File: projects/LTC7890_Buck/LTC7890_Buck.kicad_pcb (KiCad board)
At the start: 4 copper layers, 86 x 54 mm, 94 parts, among them J1 Bat In, J2 24V Out, J3 I2C Socket, J4 I2C Socket, Q1 IGC025S08S1, Q2 IGC025S08S1, Q3 IGC025S08S1, Q4 IGC025S08S1, SW1 Addr_Switch, SW2 Addr_Switch, U1 LTC7890, U2 TLV74033, U3 INA226

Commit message: Finished PCB
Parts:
- added C16: 100nF, Capacitor_SMD:C_0603_1608Metric, F.Cu at (148.5, 103.2)
- added C17: 100nF, Capacitor_SMD:C_0603_1608Metric, F.Cu at (150.0, 103.2)
- added C26: 100nF, Capacitor_SMD:C_0603_1608Metric, F.Cu at (130.0, 103.2)
- added C27: 100nF, Capacitor_SMD:C_0603_1608Metric, F.Cu at (131.5, 103.2)
- added C31: 100nF, Capacitor_SMD:C_0603_1608Metric, F.Cu at (140.8, 112.5)
- added C42: 100nF, Capacitor_SMD:C_0603_1608Metric, B.Cu at (140.0, 111.0)
- added NT1: NetTie_2, footprints:NetTie-2_SMD_Pad0.25mm, F.Cu at (139.8, 104.5)
- R14, R7: value 47 -> 100
- R15, R19, R3, R5: value 0 -> 1
- U3: footprint Package_SO:VSSOP-10_3x3mm_P0.5mm -> Package_SO:TSSOP-10_3x3mm_P0.5mm
- moved C35 23.5 mm to (137.2, 104.2), turned to 90 degrees
- moved C34 23.5 mm to (142.8, 104.2), turned to -90 degrees
- moved R14 22.2 mm to (138.8, 103.0), turned to 90 degrees
- moved R7 22.2 mm to (141.2, 103.0), turned to 90 degrees
- moved C22 7.57 mm to (124.0, 103.2)
- moved R30 6.02 mm to (145.2, 115.0)
- moved C23 4.61 mm to (125.5, 103.2)
- moved R25 4.53 mm to (136.2, 115.0)
- moved R31 4.53 mm to (142.2, 115.0)
- moved R34 4.26 mm to (155.5, 97.8), turned to -90 degrees
- moved R35 4.26 mm to (154.0, 97.8), turned to -90 degrees
- moved R5 3.89 mm to (146.0, 114.8)
- moved R19 3.48 mm to (134.0, 115.2)
- moved R20 3.48 mm to (134.0, 113.8)
- moved R6 3.26 mm to (146.0, 113.2)
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- renumbered C19 to C18, C20 to C19, C21 to C20, C22 to C21, C23 to C22, C24 to C23, C25 to C24, C26 to C25, C16 to C28, C17 to C29, C18 to C30, C27 to C32, C28 to C33, C29 to C34, C30 to C35, C31 to C36, C32 to C37, C33 to C38, C34 to C39, C35 to C40, C36 to C41, C37 to C43, C38 to C44, R18 to R17, R17 to R18
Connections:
- C1 pad 2: GND -> GNDPWR
- C10 pad 1: GND -> GNDPWR
- C11 pad 1: GND -> GNDPWR
- C12 pad 2: GND -> GNDPWR
- C13 pad 2: GND -> GNDPWR
- C14 pad 2: GND -> GNDPWR
- C15 pad 2: GND -> GNDPWR
- C18 pad 1: GND -> GNDPWR
- C19 pad 1: GND -> GNDPWR
- C2 pad 2: GND -> GNDPWR
- C20 pad 1: GND -> GNDPWR
- C21 pad 1: GND -> GNDPWR
- C22 pad 1: GND -> GNDPWR
- C23 pad 1: GND -> GNDPWR
- C24 pad 1: GND -> GNDPWR
- C25 pad 1: GND -> GNDPWR
- C28 pad 2: GND -> GNDPWR
- C29 pad 2: GND -> GNDPWR
- C3 pad 2: GND -> GNDPWR
- C30 pad 2: GND -> GNDPWR
- C33 pad 1: GND -> GNDPWR
- C36 pad 1: GND -> GNDA
- C37 pad 2: GND -> GNDA
- C38 pad 2: GND -> GNDA
- C4 pad 1: GND -> GNDPWR
- C40 pad 2: GND -> GNDA
- C41 pad 2: GND -> GNDA
- C43 pad 1: GND -> GNDA
- C5 pad 1: GND -> GNDPWR
- C6 pad 1: GND -> GNDPWR
- C7 pad 1: GND -> GNDPWR
- C8 pad 1: GND -> GNDPWR
- C9 pad 1: GND -> GNDPWR
- D1 pad 1: GND -> GNDA
- J1 pad : (no net) -> GNDPWR
- J1 pad 1: GND -> GNDPWR
- J2 pad : (no net) -> GNDPWR
- J2 pad 1: GND -> GNDPWR
- J3 pad 2: GND -> GNDA
- J3 pad MP: (no net) -> VDD
- J4 pad 2: GND -> GNDA
- J4 pad MP: (no net) -> VDD
- L1 pad 1: Net-(Q1-SS) -> Net-(L1-Pad1)
- L2 pad 2: Net-(Q3-SS) -> Net-(L2-Pad2)
- Q1 pad 3: Net-(Q1-SS) -> Net-(L1-Pad1)
- Q1 pad 5: Net-(Q1-SS) -> Net-(L1-Pad1)
- Q2 pad 2: Net-(Q1-SS) -> Net-(L1-Pad1)
- Q2 pad 3: GND -> GNDPWR
- Q2 pad 4: Net-(Q1-SS) -> Net-(L1-Pad1)
- Q2 pad 5: GND -> GNDPWR
- Q2 pad 6: GND -> GNDPWR
- Q3 pad 3: Net-(Q3-SS) -> Net-(L2-Pad2)
- Q3 pad 5: Net-(Q3-SS) -> Net-(L2-Pad2)
- Q4 pad 2: Net-(Q3-SS) -> Net-(L2-Pad2)
- Q4 pad 3: GND -> GNDPWR
- Q4 pad 4: Net-(Q3-SS) -> Net-(L2-Pad2)
- Q4 pad 5: GND -> GNDPWR
- Q4 pad 6: GND -> GNDPWR
- R16 pad 2: GND -> GNDA
- R2 pad 1: GND -> GNDA
- R9 pad 1: GND -> GNDA
- SW1 pad : (no net) -> GNDPWR
- SW1 pad 1: GND -> GNDA
- SW2 pad : (no net) -> GNDPWR
- SW2 pad 1: GND -> GNDA
- TP2 pad 1: GND -> GNDPWR
- TP4 pad 1: GND -> GNDPWR
- U1 pad 14: GND -> GNDA
- U1 pad 15: GND -> GNDA
- U1 pad 26: +24V -> VOUT
- U1 pad 3: GND -> GNDA
- U1 pad 41: GND -> GNDPWR
- U1 pad 6: GND -> GNDA
- U1 pad 7: GND -> unconnected-(U1-DRVUV-Pad7)
- U1 pad 8: GND -> GNDA
- U2 pad 2: GND -> GNDA
- U3 pad 7: GND -> GNDA
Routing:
- net Net-(J3-Pin_3): track 0.00 -> 88.3 mm, vias 0 -> 3
- net GNDA: track 0.00 -> 87.9 mm, vias 0 -> 8
- net Net-(J3-Pin_4): track 0.00 -> 84.2 mm, vias 0 -> 3
- net VOUT: track 0.00 -> 80.6 mm, vias 0 -> 6
- net +3.3V: track 0.00 -> 61.3 mm, vias 0 -> 2
- net +5V: track 0.00 -> 42.8 mm, vias 0 -> 3
- net /R-: track 0.00 -> 38.4 mm, vias 0 -> 2
- net Net-(U3-A0): track 0.00 -> 37.5 mm, vias 0 -> 1
- net Net-(L2-Pad1): track 0.00 -> 36.3 mm, vias 0 -> 2
- net Net-(L1-Pad2): track 0.00 -> 34.4 mm, vias 0 -> 2
- net /R+: track 0.00 -> 34.3 mm, vias 0 -> 2
- net Net-(U3-A1): track 0.00 -> 20.3 mm
- net /~{Alert}: track 0.00 -> 18.4 mm, vias 0 -> 2
- net VDD: track 0.00 -> 12.0 mm, vias 0 -> 27
- net Net-(R25-Pad1): track 0.00 -> 11.0 mm, vias 0 -> 2
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- added copper zone on B.Cu, net +24V
- added copper zone on F.Cu, net +24V
- added copper zone on B.Cu, net GNDA
- added copper zone on F.Cu, net GNDA
- added copper zone on B.Cu, net GNDPWR
- added copper zone on F.Cu, net GNDPWR
- added copper zone on In1.Cu, net GNDPWR
- added copper zone on In2.Cu, net GNDPWR
- added copper zone on F.Cu, net Net-(L1-Pad1)
- added copper zone on F.Cu, net Net-(L2-Pad2)
- added copper zone on F.Cu, net Net-(Q1-G)
- added copper zone on F.Cu, net Net-(Q1-SS)
- added copper zone on F.Cu, net Net-(Q2-G)
- added copper zone on F.Cu, net Net-(Q3-G)
- added copper zone on F.Cu, net Net-(Q3-SS)
- added copper zone on F.Cu, net Net-(Q4-G)
- added copper zone on B.Cu, net VDD
- added copper zone on F.Cu, net VDD
- added copper zone on B.Cu, net VOUT

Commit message: Minor changes
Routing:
- net GNDA: track 87.9 -> 86.7 mm
- net GNDPWR: vias 222 -> 226
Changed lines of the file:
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@@
 		(at 148.75 121.5 90)
 		(property "Reference" "R26"
-			(at 4.5 -2 0)
+			(at -4.5 -2 0)
 			(unlocked yes)
 			(layer "B.SilkS")
@@
 		(at 135.25 121.5 90)
 		(property "Reference" "R29"
-			(at 4.5 -1.75 0)
+			(at -4.5 -1.75 0)
 			(unlocked yes)
 			(layer "B.SilkS")
@@
 		(at 144.25 121.5 90)
 		(property "Reference" "R27"
-			(at 4.5 -2 0)
+			(at -4.5 -2 0)
 			(unlocked yes)
 			(layer "B.SilkS")
@@
 		(at 139.75 121.5 90)
 		(property "Reference" "R28"
-			(at 4.5 -2 0)
+			(at -4.5 -2 0)
 			(unlocked yes)
 			(layer "B.SilkS")
@@
 	)
 	(via
+		(at 134 112)
+		(size 0.6)
+		(drill 0.3)
+		(layers "F.Cu" "B.Cu")
+		(free yes)
+		(net "GNDPWR")
+	)
+	(via
 		(at 122.5 88)
 		(size 0.6)
@@
 	)
 	(via
+		(at 133.25 112.5)
+		(size 0.6)
+		(drill 0.3)
+		(layers "F.Cu" "B.Cu")
+		(free yes)
+		(net "GNDPWR")
+	)
+	(via
 		(at 105 116)
 		(size 0.6)
@@
 	)
 	(via
+		(at 132.5 112)
+		(size 0.6)
+		(drill 0.3)
+		(layers "F.Cu" "B.Cu")
+		(free yes)
+		(net "GNDPWR")
+	)
+	(via
 		(at 157.5 88)
 		(size 0.6)
@@
 	)
 	(via
+		(at 134.75 112.5)
+		(size 0.6)
+		(drill 0.3)
+		(layers "F.Cu" "B.Cu")
+		(free yes)
+		(net "GNDPWR")
+	)
+	(via
 		(at 145 132)
 		(size 0.6)
@@
 	)
 	(segment
-		(start 137.0625 106)
+		(start 137.0625 106.5)
 		(end 137.0625 106.25)
 		(width 0.25)
@@
 	)
 	(segment
+		(start 136.25 106.25)
+		(end 137.0625 106.25)
+		(width 0.5)
+		(layer "F.Cu")
+		(net "GNDA")
+	)
+	(segment
+		(start 137.0625 106.25)
+		(end 137.0625 106)
+		(width 0.25)
+		(layer "F.Cu")
+		(net "GNDA")
+	)
+	(segment
 		(start 178.499999 98.875)
 		(end 177.65 98.875)
@@
 	)
 	(segment
-		(start 137.0625 106.25)
-		(end 137.0625 106.5)
-		(width 0.25)
-		(layer "F.Cu")
-		(net "GNDA")
-	)
-	(segment
 		(start 177.65 88.875)
 		(end 178.375 88.875)
@@
 	)
 	(segment
-		(start 137.0625 106.25)
-		(end 136.5 106.25)
-		(width 0.25)
-		(layer "F.Cu")
-		(net "GNDA")
-	)
-	(segment
 		(start 163.25 101.5)
 		(end 174.25 101.5)
@@
 	)
 	(via
-		(at 136.5 106.25)
+		(at 136.25 106.25)
 		(size 0.6)
 		(drill 0.3)
@@
 	)
 	(segment
-		(start 136.5 106.25)
-		(end 137.5 105.25)
-		(width 0.5)
-		(layer "In1.Cu")
-		(net "GNDA")
-	)
-	(segment
 		(start 137.5 105.25)
 		(end 137.5 101.25)
@@
 	)
 	(segment
-		(start 144.825 115.825)
-		(end 144.825 104.741116)
+		(start 152.75 123.75)
+		(end 144.825 115.825)
 		(width 0.25)
 		(layer "In2.Cu")
@@
 	)
 	(segment
-		(start 144.825 104.741116)
-		(end 143.833884 103.75)
+		(start 153.5 126)
+		(end 153.5 125)
 		(width 0.25)
 		(layer "In2.Cu")
@@
 	)
 	(segment
-		(start 127.25 123.25)
-		(end 137.125 113.375)
+		(start 144.825 115.825)
+		(end 144.825 104.741116)
 		(width 0.25)
 		(layer "In2.Cu")
@@
 	)
 	(segment
-		(start 149 120)
-		(end 144.825 115.825)
+		(start 127.25 123.25)
+		(end 137.125 113.375)
 		(width 0.25)
 		(layer "In2.Cu")
@@
 	)
 	(segment
-		(start 143.833884 103.75)
-		(end 143.75 103.75)
+		(start 152.75 124.25)
+		(end 152.75 123.75)
+		(width 0.25)
+		(layer "In2.Cu")
+		(net "VOUT")
+	)
+	(segment
+		(start 144.825 104.741116)
+		(end 143.833884 103.75)
 		(width 0.25)
 		(layer "In2.Cu")
@@
 	)
 	(segment
-		(start 149 121.5)
-		(end 149 120)
+		(start 143.833884 103.75)
+		(end 143.75 103.75)
 		(width 0.25)
 		(layer "In2.Cu")
@@
 	)
 	(segment
-		(start 126.5 126)
-		(end 125.75 125.25)
+		(start 153.5 125)
+		(end 152.75 124.25)
 		(width 0.25)
 		(layer "In2.Cu")
@@
 	)
 	(segment
-		(start 126.25 123.25)
-		(end 127.25 123.25)
+		(start 126.5 126)
+		(end 125.75 125.25)
 		(width 0.25)
 		(layer "In2.Cu")
@@
 	)
 	(segment
-		(start 153.5 126)
-		(end 149 121.5)
+		(start 126.25 123.25)
+		(end 127.25 123.25)
 		(width 0.25)
 		(layer "In2.Cu")
@@
 	)
 	(segment
+		(start 135.933058 105.5)
+		(end 135.625 105.808058)
+		(width 0.25)
+		(layer "F.Cu")
+		(net "+5V")
+	)
+	(segment
 		(start 134.75 103)
 		(end 135.75 102)
@@
 	)
 	(segment
-		(start 141.5 100.425)
-		(end 141.5 99.5)
+		(start 135.889514 107)
+		(end 137.0625 107)
 		(width 0.25)
 		(layer "F.Cu")
@@
 	)
 	(segment
-		(start 136.183884 102)
-		(end 135.75 102)
+		(start 141.5 100.425)
+		(end 141.5 99.5)
 		(width 0.25)
 		(layer "F.Cu")
@@
 	)
 	(segment
-		(start 134.75 104.925)
-		(end 135.05 104.925)
+		(start 137.0625 105.5)
+		(end 135.933058 105.5)
 		(width 0.25)
 		(layer "F.Cu")
@@
 	)
 	(segment
-		(start 135.875 105.75)
-		(end 136.125 105.5)
+		(start 136.183884 102)
+		(end 135.75 102)
 		(width 0.25)
 		(layer "F.Cu")
@@
 	)
 	(segment
-		(start 136.125 107)
-		(end 137.0625 107)
+		(start 135.625 106.735486)
+		(end 135.889514 107)
 		(width 0.25)
 		(layer "F.Cu")
@@
 	)
 	(segment
-		(start 135.05 104.925)
-		(end 135.875 105.75)
+		(start 134.75 104.925)
+		(end 135.625 105.8)
 		(width 0.25)
 		(layer "F.Cu")
@@
 	)
 	(segment
-		(start 136.125 105.5)
-		(end 137.0625 105.5)
-		(width 0.25)
+		(start 139.25 111.75)
+		(end 138.5 112.5)
+		(width 0.2)
 		(layer "F.Cu")
 		(net "+5V")
 	)
 	(segment
-		(start 135.875 106.75)
-		(end 136.125 107)
+		(start 137.75 103.8125)
+		(end 137.75 103.566116)
 		(width 0.25)
 		(layer "F.Cu")
@@
 	)
 	(segment
-		(start 139.25 111.75)
-		(end 138.5 112.5)
-		(width 0.2)
+		(start 135.625 105.808058)
+		(end 135.625 105.933058)
+		(width 0.25)
 		(layer "F.Cu")
 		(net "+5V")
 	)
 	(segment
-		(start 137.75 103.8125)
-		(end 137.75 103.566116)
+		(start 135.625 105.8)
+		(end 135.625 106.735486)
 		(width 0.25)
 		(layer "F.Cu")
@@
 		(net "+5V")
 	)
-	(segment
-		(start 135.875 106.75)
-		(end 135.875 105.75)
-		(width 0.25)
-		(layer "F.Cu")
-		(net "+5V")
-	)
 	(via
 		(at 138.5 112.5)
@@
 		(layer "F.Cu")
 		(hatch edge 0.5)
-		(priority 15)
+		(priority 13)
 		(connect_pads
 			(clearance 0.2)
@@
 		(layer "F.Cu")
 		(hatch edge 0.5)
-		(priority 13)
+		(priority 12)
 		(connect_pads
 			(clearance 0.2)
@@
 		(layer "F.Cu")
 		(hatch edge 0.5)
-		(priority 11)
+		(priority 10)
 		(connect_pads
 			(clearance 0.2)
@@
 		(layer "B.Cu")
 		(hatch edge 0.5)
-		(priority 16)
+		(priority 18)
 		(connect_pads
 			(clearance 0.2)
@@
 		(layer "B.Cu")
 		(hatch edge 0.5)
-		(priority 10)
+		(priority 15)
 		(connect_pads
 			(clearance 0.2)
@@
 		(layer "B.Cu")
 		(hatch edge 0.5)
-		(priority 10)
+		(priority 14)
 		(connect_pads
 			(clearance 0.2)
@@
 		(layer "B.Cu")
 		(hatch edge 0.5)
-		(priority 12)
+		(priority 16)
 		(connect_pads
 			(clearance 0.2)
@@
 		(layer "B.Cu")
 		(hatch edge 0.5)
-		(priority 14)
+		(priority 17)
 		(connect_pads
 			(clearance 0.2)

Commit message: Minor changes 2
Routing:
- net GNDA: track 86.7 -> 88.2 mm
- net GNDPWR: vias 226 -> 224
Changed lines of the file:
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@@
 			)
 		)
+		(solder_paste_margin -0.05)
 		(attr smd)
 		(duplicate_pad_numbers_are_jumpers no)
@@
 			)
 		)
+		(solder_paste_margin -0.05)
 		(attr smd)
 		(duplicate_pad_numbers_are_jumpers no)
@@
 	)
 	(via
-		(at 150 132)
-		(size 0.6)
-		(drill 0.3)
-		(layers "F.Cu" "B.Cu")
-		(free yes)
-		(net "GNDPWR")
-	)
-	(via
 		(at 152.5 136)
 		(size 0.6)
@@
 	)
 	(via
-		(at 130 132)
-		(size 0.6)
-		(drill 0.3)
-		(layers "F.Cu" "B.Cu")
-		(free yes)
-		(net "GNDPWR")
-	)
-	(via
 		(at 102.5 88)
 		(size 0.6)
@@
 	)
 	(segment
+		(start 136.25 106.25)
+		(end 137 105.5)
+		(width 0.5)
+		(layer "In1.Cu")
+		(net "GNDA")
+	)
+	(segment
+		(start 137 101.75)
+		(end 137.5 101.25)
+		(width 0.5)
+		(layer "In1.Cu")
+		(net "GNDA")
+	)
+	(segment
 		(start 144 101.25)
 		(end 145 102.25)
@@
 	)
 	(segment
-		(start 137.5 105.25)
-		(end 137.5 101.25)
+		(start 137 105.5)
+		(end 137 101.75)
 		(width 0.5)
 		(layer "In1.Cu")
@@
 	)
 	(segment
-		(start 147.25 97.25)
-		(end 119 97.25)
+		(start 154.75 97.75)
+		(end 154.25 97.75)
 		(width 0.25)
 		(layer "In2.Cu")
@@
 	)
 	(segment
-		(start 153.25 96.25)
-		(end 148.25 96.25)
+		(start 147.25 97.25)
+		(end 119 97.25)
+		(width 0.25)
+		(layer "In2.Cu")
+		(net "Net-(J3-Pin_3)")
+	)
+	(segment
+		(start 154.25 97.75)
+		(end 153 96.5)
 		(width 0.25)
 		(layer "In2.Cu")
@@
 	)
 	(segment
-		(start 154.75 97.75)
-		(end 153.25 96.25)
+		(start 119 97.25)
+		(end 116.25 100)
 		(width 0.25)
 		(layer "In2.Cu")
@@
 	)
 	(segment
-		(start 148.25 96.25)
-		(end 147.25 97.25)
+		(start 153 96.5)
+		(end 148 96.5)
 		(width 0.25)
 		(layer "In2.Cu")
@@
 	)
 	(segment
-		(start 119 97.25)
-		(end 116.25 100)
+		(start 148 96.5)
+		(end 147.25 97.25)
 		(width 0.25)
 		(layer "In2.Cu")
@@
 	)
 	(segment
-		(start 137 104.5)
-		(end 136.25 103.75)
+		(start 140 110.75)
+		(end 140.25 110.5)
 		(width 0.25)
 		(layer "F.Cu")
@@
 	)
 	(segment
-		(start 143 104.5)
-		(end 143.75 103.75)
+		(start 137 104.5)
+		(end 136.25 103.75)
 		(width 0.25)
 		(layer "F.Cu")
@@
 	)
 	(segment
-		(start 140 110.75)
-		(end 140.25 110.5)
+		(start 143 104.5)
+		(end 143.75 103.75)
 		(width 0.25)
 		(layer "F.Cu")
@@
 	)
 	(segment
-		(start 140 110.75)
-		(end 140 110.225)
-		(width 0.25)
-		(layer "B.Cu")
-		(net "VOUT")
-	)
-	(segment
 		(start 143.475 103.475)
 		(end 143.75 103.75)
@@
 	)
 	(segment
+		(start 140 110.75)
+		(end 140 110.225)
+		(width 0.25)
+		(layer "B.Cu")
+		(net "VOUT")
+	)
+	(segment
 		(start 153.5 127.6)
 		(end 153.5 126)
@@
 	)
 	(segment
-		(start 140 110.75)
-		(end 140 112.75)
+		(start 141.75 118.25)
+		(end 141 119)
 		(width 0.5)
 		(layer "In1.Cu")
@@
 	)
 	(segment
-		(start 141.75 114.5)
-		(end 141.75 118.25)
+		(start 140 123)
+		(end 140 126)
 		(width 0.5)
 		(layer "In1.Cu")
@@
 	)
 	(segment
-		(start 141 122)
-		(end 140 123)
+		(start 140 110.75)
+		(end 140 112.75)
 		(width 0.5)
 		(layer "In1.Cu")
@@
 	(segment
 		(start 141 122)
-		(end 141 119)
+		(end 140 123)
 		(width 0.5)
 		(layer "In1.Cu")
@@
 	)
 	(segment
-		(start 141 119)
+		(start 141.75 114.5)
 		(end 141.75 118.25)
 		(width 0.5)
@@
 	)
 	(segment
-		(start 140 123)
-		(end 140 126)
+		(start 141 119)
+		(end 141 122)
 		(width 0.5)
 		(layer "In1.Cu")
@@
 	)
 	(segment
-		(start 134.75 104.925)
-		(end 134.75 103)
-		(width 0.25)
-		(layer "F.Cu")
-		(net "+5V")
-	)
-	(segment
 		(start 135.933058 105.5)
 		(end 135.625 105.808058)
@@
 	)
 	(segment
-		(start 134.75 103)
-		(end 135.75 102)
+		(start 134.75 104.925)
+		(end 135.25 104.425)
 		(width 0.25)
 		(layer "F.Cu")
@@
 	)
 	(segment
+		(start 135.25 102.5)
+		(end 135.75 102)
+		(width 0.25)
+		(layer "F.Cu")
+		(net "+5V")
+	)
+	(segment
 		(start 138.25 103.8125)
 		(end 137.75 103.8125)
@@
 	)
 	(segment
-		(start 134.75 104.925)
-		(end 135.625 105.8)
-		(width 0.25)
-		(layer "F.Cu")
-		(net "+5V")
-	)
-	(segment
 		(start 139.25 111.75)
 		(end 138.5 112.5)
@@
 	)
 	(segment
-		(start 135.625 105.808058)
-		(end 135.625 105.933058)
+		(start 135.25 104.425)
+		(end 135.25 102.5)
 		(width 0.25)
 		(layer "F.Cu")
@@
 		(width 0.25)
 		(layer "F.Cu")
+		(net "+5V")
+	)
+	(segment
+		(start 134.75 104.925)
+		(end 135.625 105.8)
+		(width 0.25)
+		(layer "F.Cu")

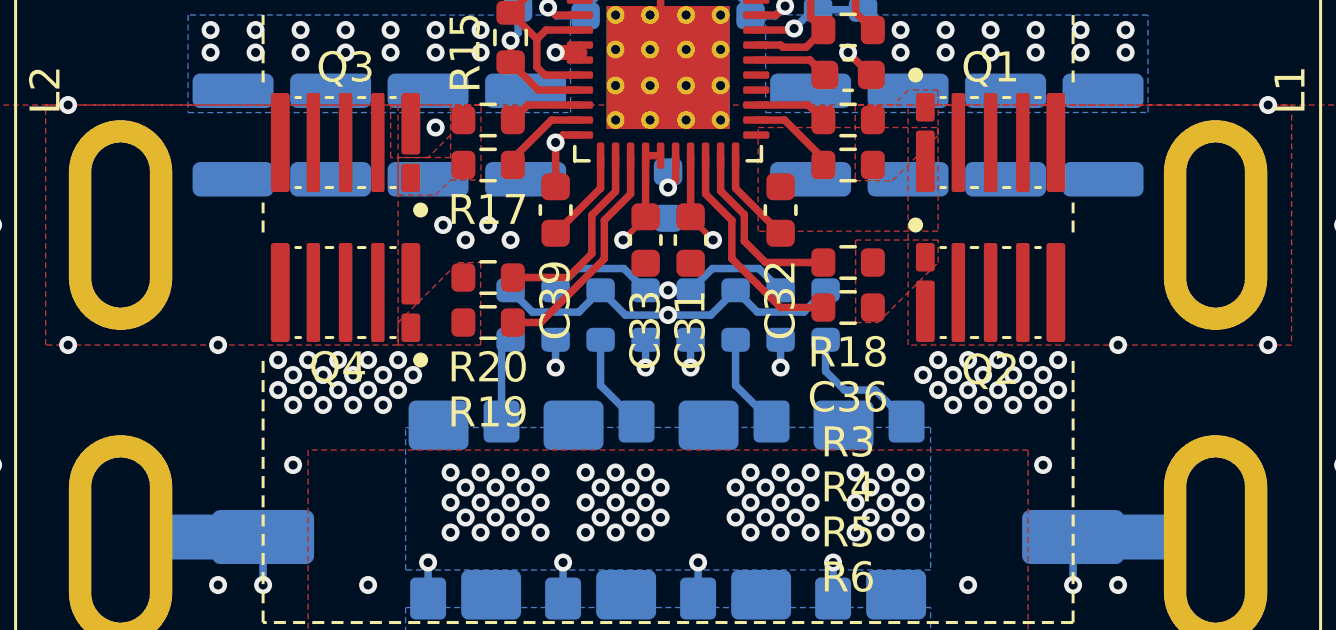
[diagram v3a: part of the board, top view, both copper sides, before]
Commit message: Added low side fet diode
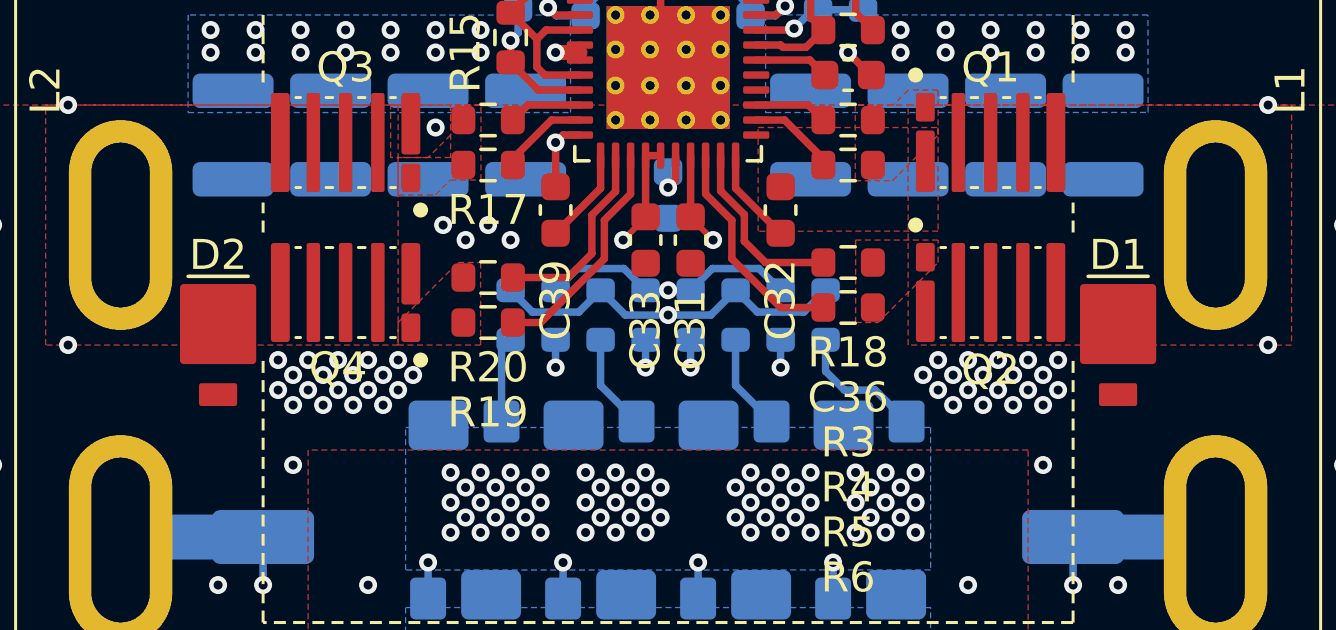
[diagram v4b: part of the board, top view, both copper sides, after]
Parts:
- added D1: V3PM10, footprints:D_SMP_DO-220AA, F.Cu at (155.0, 116.0)
- added D2: V3PM10, footprints:D_SMP_DO-220AA, F.Cu at (125.0, 116.0)
- renumbered D1 to D3
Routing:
- net GNDPWR: vias 224 -> 222

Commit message: Minor changes again
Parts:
- R15, R3: value 1 -> 2.2
- moved R22 0.50 mm to (143.8, 115.5)
- moved R23 0.50 mm to (140.8, 115.5)
- moved R24 0.50 mm to (139.2, 115.5)
- moved R25 0.50 mm to (136.2, 115.5)
- moved R30 0.50 mm to (145.2, 115.5)
- moved R31 0.50 mm to (142.2, 115.5)
- moved R32 0.50 mm to (137.8, 115.5)
- moved R33 0.50 mm to (134.8, 115.5)
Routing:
- net Net-(R29-Pad3): track 2.85 -> 2.35 mm
- net Net-(R28-Pad3): track 3.22 -> 2.72 mm
- net Net-(R27-Pad3): track 3.22 -> 2.72 mm
- net Net-(R26-Pad3): track 4.44 -> 3.94 mm
- net Net-(R24-Pad1): track 9.76 -> 9.26 mm
- net Net-(R23-Pad1): track 8.73 -> 8.23 mm
- net Net-(R22-Pad1): track 9.35 -> 8.85 mm
- net GNDPWR: vias 222 -> 232
